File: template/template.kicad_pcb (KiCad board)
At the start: 2 copper layers, 75 x 55 mm, 41 parts, among them J1 Network Connector, J3 STDC14 STLink connector, SW1 SW_Push, U1 LD39050PU33R, U2 STM32G474RBT6, U3 SN65HVD230, Y1 8MHz

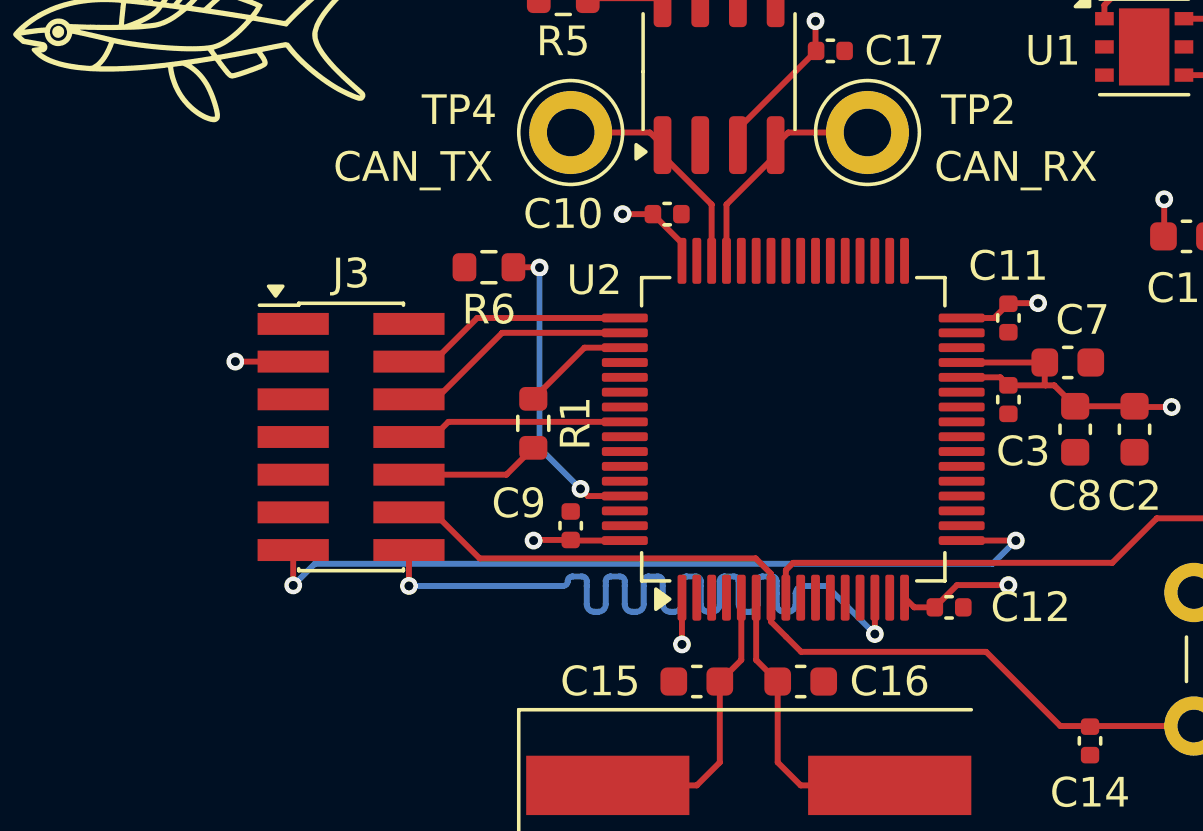
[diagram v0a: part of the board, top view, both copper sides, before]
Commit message: template: rearrange traces near STDC14 STLink connector
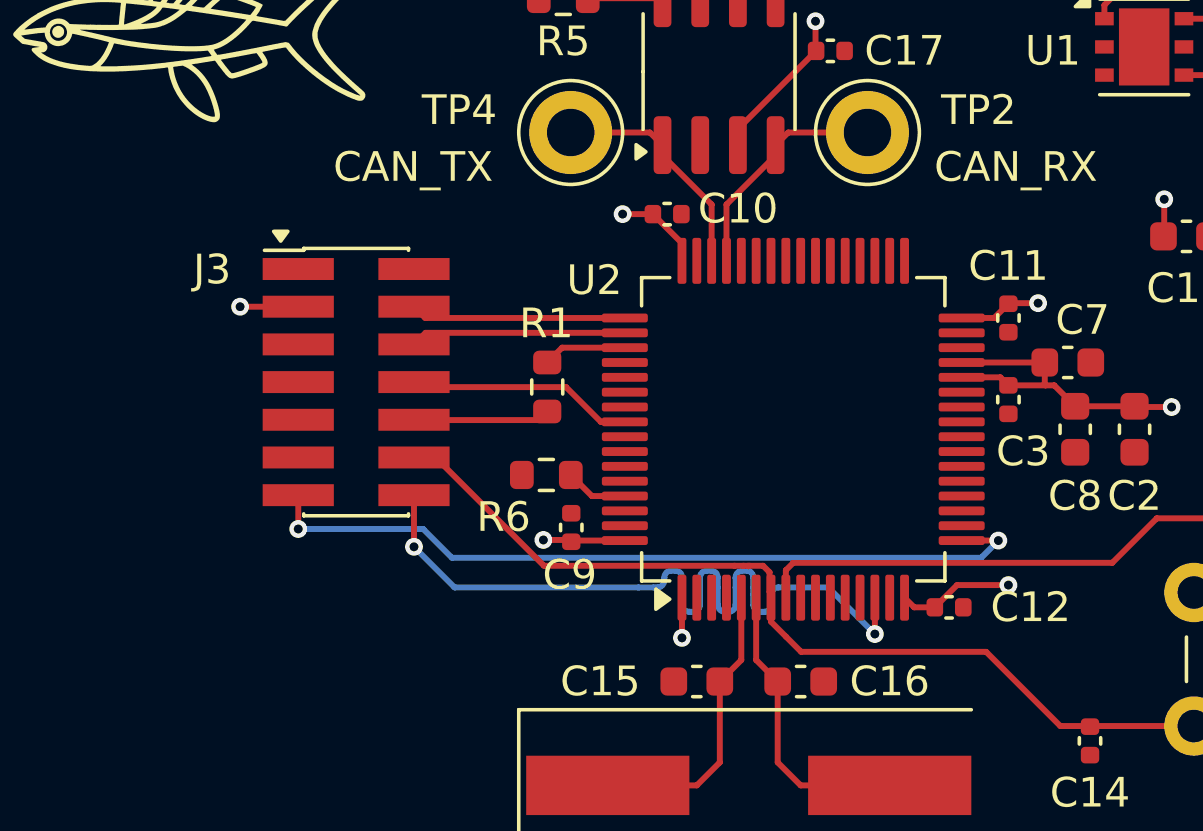
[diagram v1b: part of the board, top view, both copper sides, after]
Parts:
- J3: value STDC14 STLink connector -> STDC14
- moved R6 7.26 mm to (209.9, 53.3)
- moved J3 1.86 mm to (203.5, 50.2)
- moved R1 1.31 mm to (210.0, 50.3)
- moved C9 0.06 mm to (210.8, 55.1)
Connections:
- SW1 pad 1: GND -> /STM32 Base Layout/T_NRST
- SW1 pad 2: /STM32 Base Layout/T_NRST -> GND
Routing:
- net Net-(U2-PB8): track 10.5 -> 2.11 mm, vias 2 -> 0
- net /STM32 Base Layout/T_VCP_TX: track 30.6 -> 26.5 mm
- net /STM32 Base Layout/T_VCP_RX: track 28.0 -> 26.6 mm
- net Net-(U2-PA15): track 3.80 -> 2.82 mm
- net /STM32 Base Layout/T_JCLK/T_SWCLK: track 8.20 -> 7.27 mm
- net /STM32 Base Layout/T_JTMS/T_SWDIO: track 7.88 -> 7.26 mm
- net /STM32 Base Layout/T_NRST: track 36.9 -> 37.5 mm
- net +3.3V: track 45.2 -> 44.7 mm

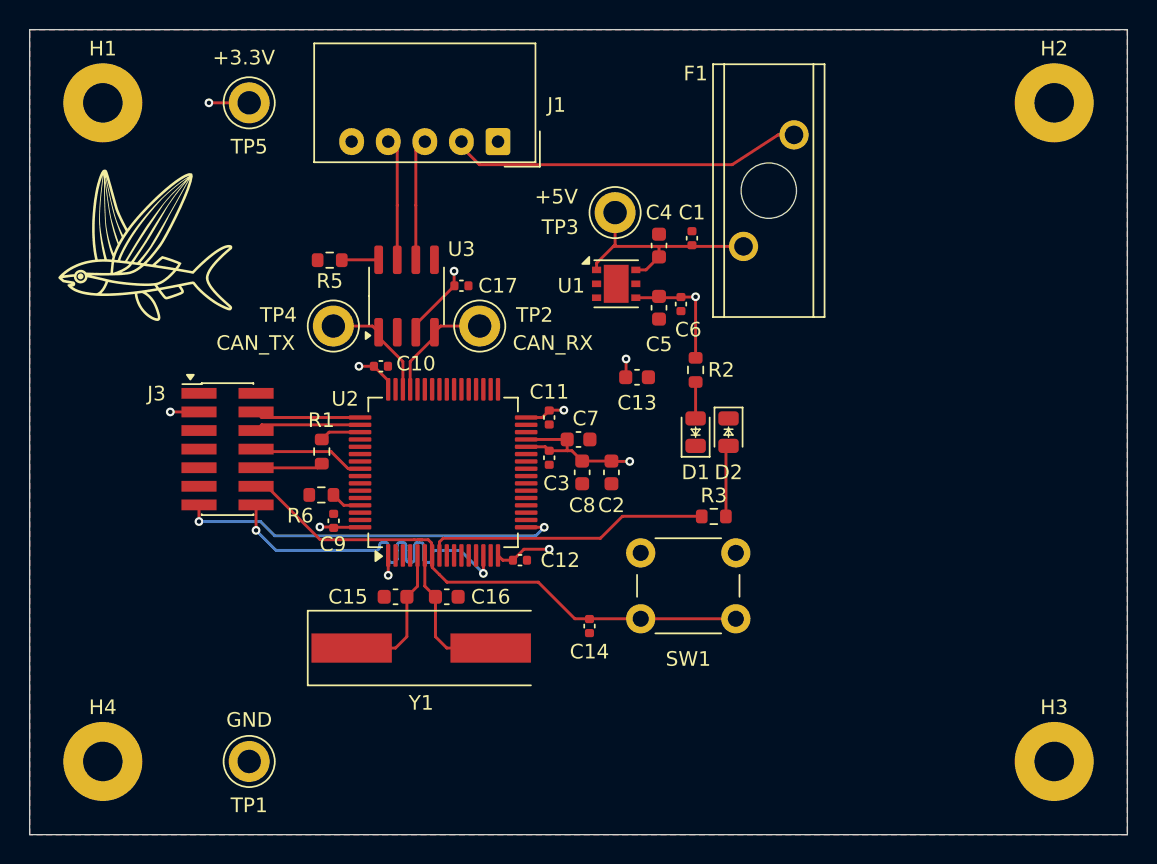
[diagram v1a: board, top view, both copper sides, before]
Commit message: template: parts placement optimisation
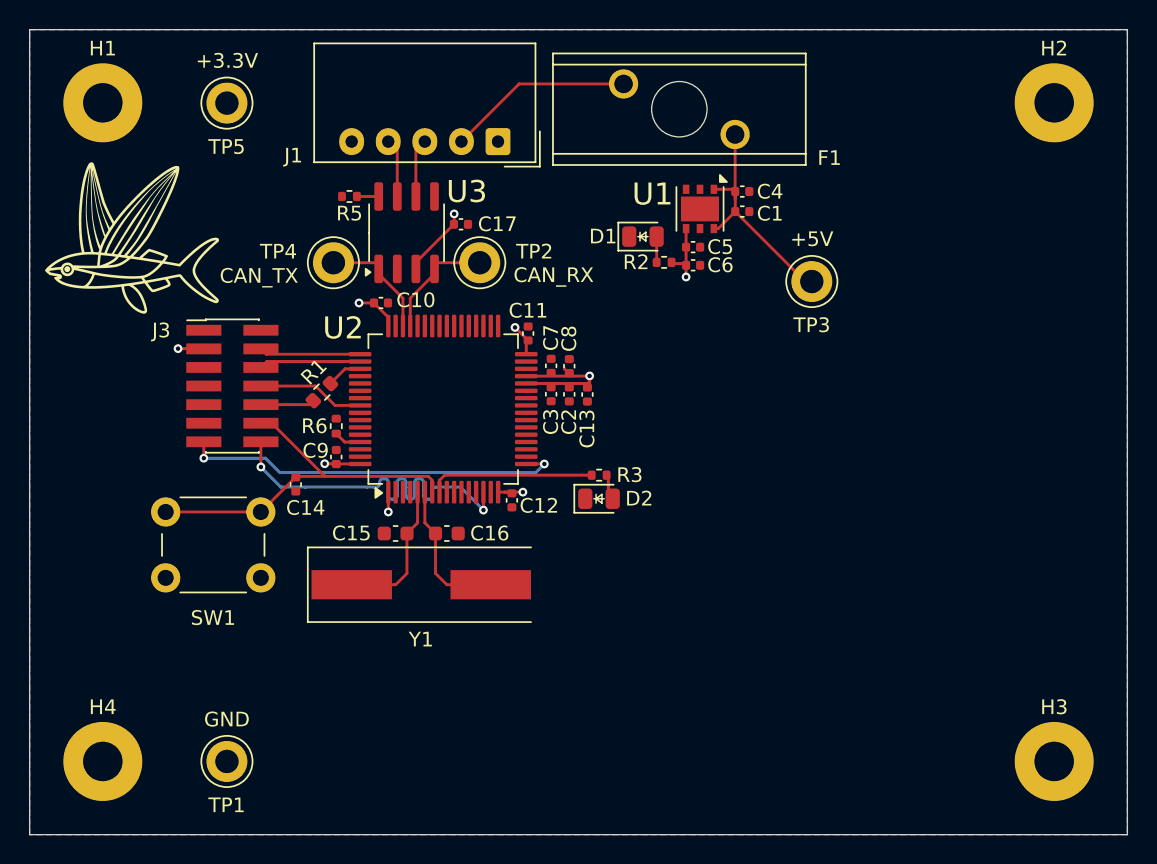
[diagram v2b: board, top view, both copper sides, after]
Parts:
- C13, C2, C4, C5, C7, C8: footprint Capacitor_SMD:C_0603_1608Metric -> Capacitor_SMD:C_0402_1005Metric
- R2, R3, R5, R6: footprint Resistor_SMD:R_0603_1608Metric -> Resistor_SMD:R_0402_1005Metric
- moved SW1 32.6 mm to (199.3, 54.5)
- moved C14 22.3 mm to (208.2, 52.6)
- moved TP3 14.2 mm to (243.4, 38.7)
- moved D1 13.8 mm to (231.9, 35.6), turned to 0 degrees
- moved D2 9.95 mm to (228.9, 53.5), turned to 0 degrees
- moved R3 8.33 mm to (228.9, 51.9)
- moved F1 8.26 mm to (234.4, 26.9), turned to 90 degrees
- moved U1 7.68 mm to (235.8, 33.8), turned to -90 degrees
- moved R2 7.66 mm to (233.3, 37.4), turned to 180 degrees
- moved C8 7.31 mm to (226.9, 44.5), turned to 90 degrees
- moved C4 6.78 mm to (238.7, 32.6), turned to 0 degrees
- moved C2 6.06 mm to (226.9, 46.4)
- moved C11 5.92 mm to (224.1, 42.3), turned to 90 degrees
- moved C7 5.37 mm to (225.6, 44.5), turned to 90 degrees
- moved R6 4.81 mm to (210.9, 48.6), turned to 90 degrees
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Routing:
- net +3.3V: track 44.7 -> 31.9 mm, vias 11 -> 9
- net /STM32 Base Layout/T_NRST: track 37.5 -> 26.3 mm
- net Net-(J1-+5V): track 23.8 -> 12.7 mm
- net /STM32 Base Layout/STATUS_LED: track 19.6 -> 11.3 mm
- net /STM32 Base Layout/CAN_L: track 8.33 -> 4.36 mm
- net /STM32 Base Layout/CAN_H: track 8.33 -> 4.37 mm
- net Net-(D2-A): track 4.88 -> 1.78 mm
- net Net-(U3-Rs): track 2.53 -> 1.49 mm
- net +5V: track 16.0 -> 15.2 mm
- net Net-(D1-A): track 2.49 -> 1.76 mm
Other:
- board text removed: "+3.3V"
- board text removed: "+5V"
- board text removed: "CAN_RX"
- board text removed: "CAN_TX"
- board text removed: "GND"

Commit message: template: labels, traces, & parts placement corrections
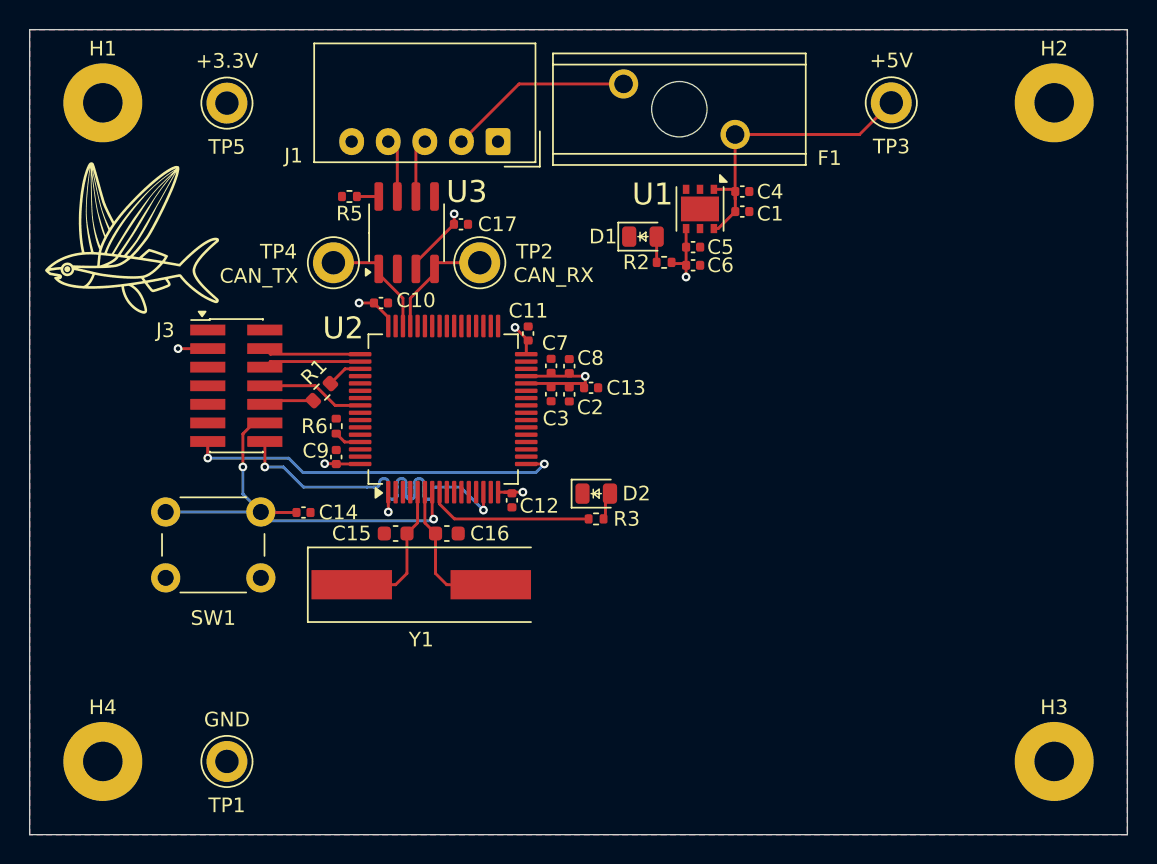
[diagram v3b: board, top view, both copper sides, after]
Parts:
- moved TP3 13.4 mm to (248.9, 26.5)
- moved R3 3.00 mm to (228.7, 54.9)
- moved C14 1.99 mm to (208.7, 54.5), turned to 180 degrees
- moved C13 0.52 mm to (228.4, 46.0), turned to 0 degrees
- moved D2 0.40 mm to (228.7, 53.2)
- moved J3 0.27 mm to (204.1, 45.8)
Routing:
- net +5V: track 15.2 -> 20.8 mm
- net /STM32 Base Layout/T_NRST: track 26.3 -> 30.8 mm, vias 0 -> 2
- net +3.3V: track 31.9 -> 30.4 mm

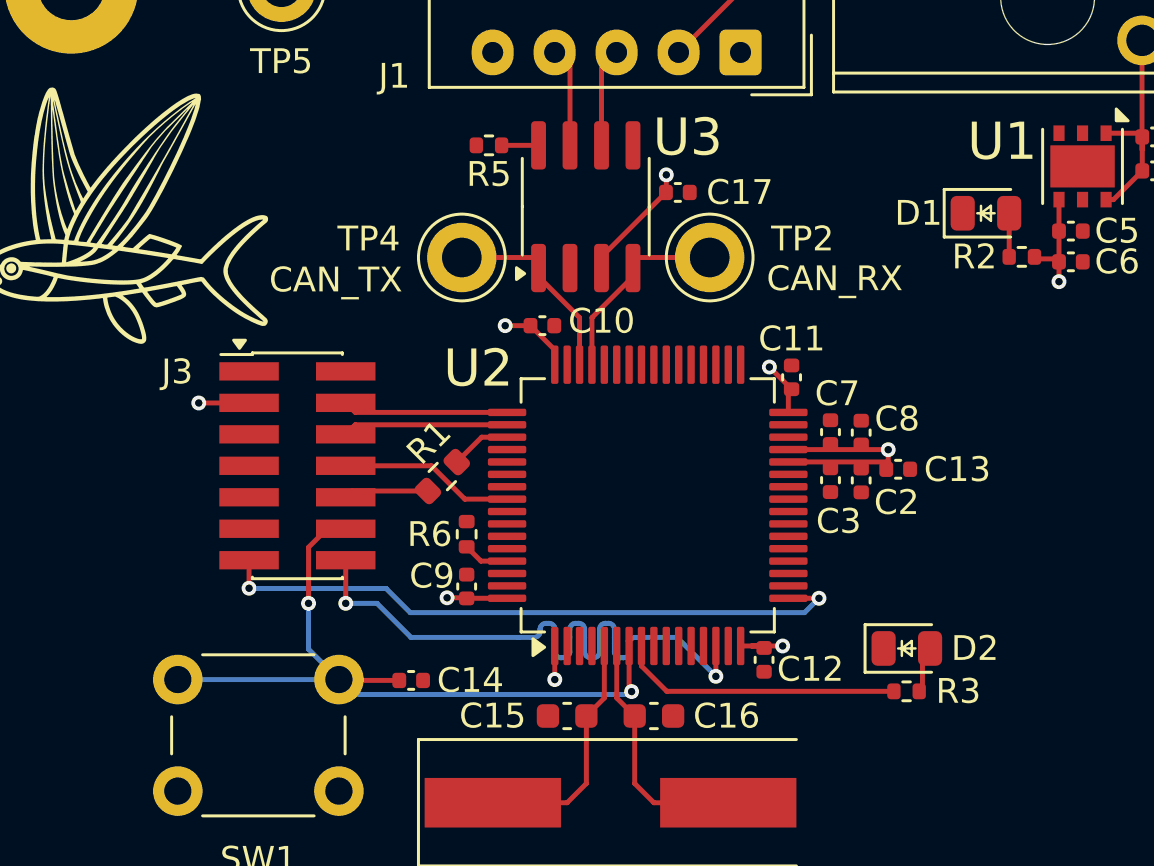
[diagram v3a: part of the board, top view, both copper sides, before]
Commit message: template: re-reference all components
Had to re-add R1 and J2, but they were replaced where they were.
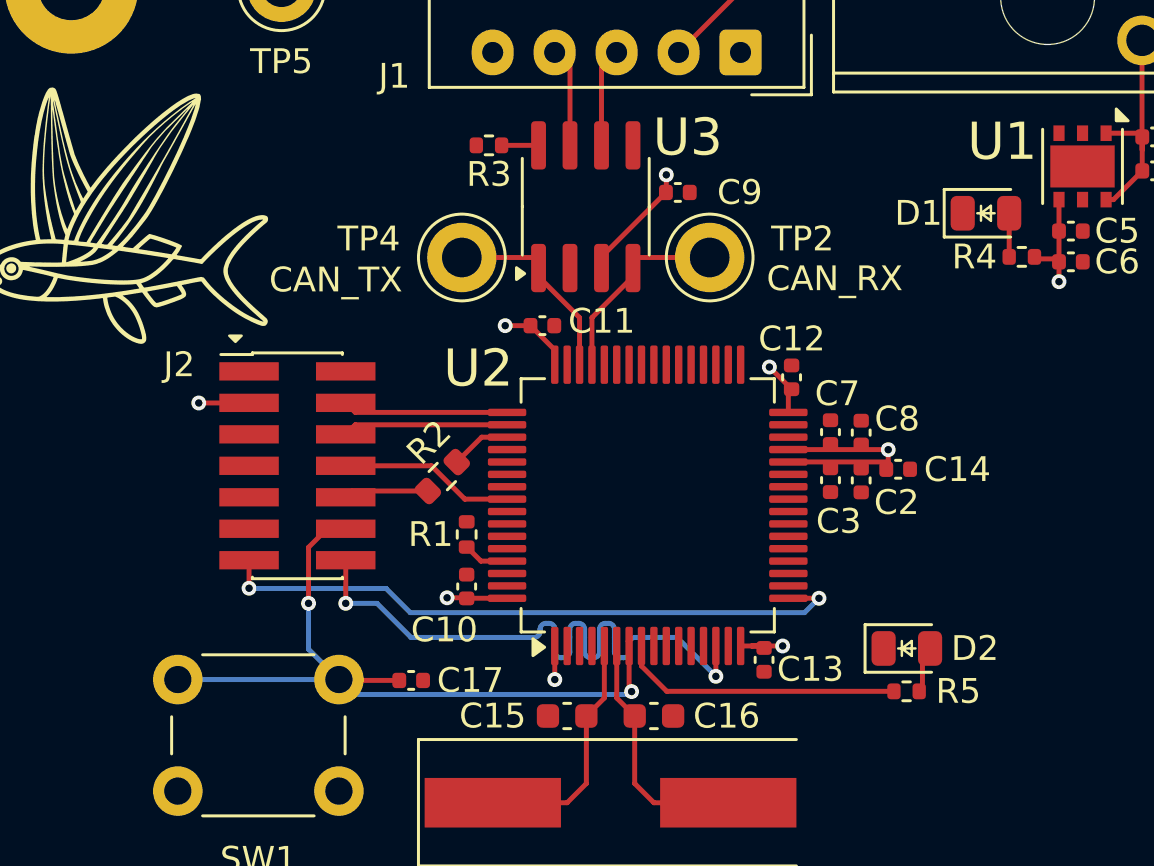
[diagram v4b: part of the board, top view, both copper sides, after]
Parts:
- removed J3: STDC14, Connector_PinHeader_1.27mm:PinHeader_2x07_P1.27mm_Vertical_SMD
- removed R6: 10k, Resistor_SMD:R_0402_1005Metric
- added J2: STDC14, Connector_PinHeader_1.27mm:PinHeader_2x07_P1.27mm_Vertical_SMD, F.Cu at (204.1, 45.8)
- added R1: 10k, Resistor_SMD:R_0402_1005Metric, F.Cu at (210.9, 48.6)
- renumbered C9 to C10, C10 to C11, C11 to C12, C12 to C13, C13 to C14, C14 to C17, C17 to C9, R1 to R2, R5 to R3, R2 to R4, R3 to R5
